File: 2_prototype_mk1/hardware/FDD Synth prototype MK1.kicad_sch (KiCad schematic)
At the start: 3 parts, among them J3 Conn_01x04_Pin

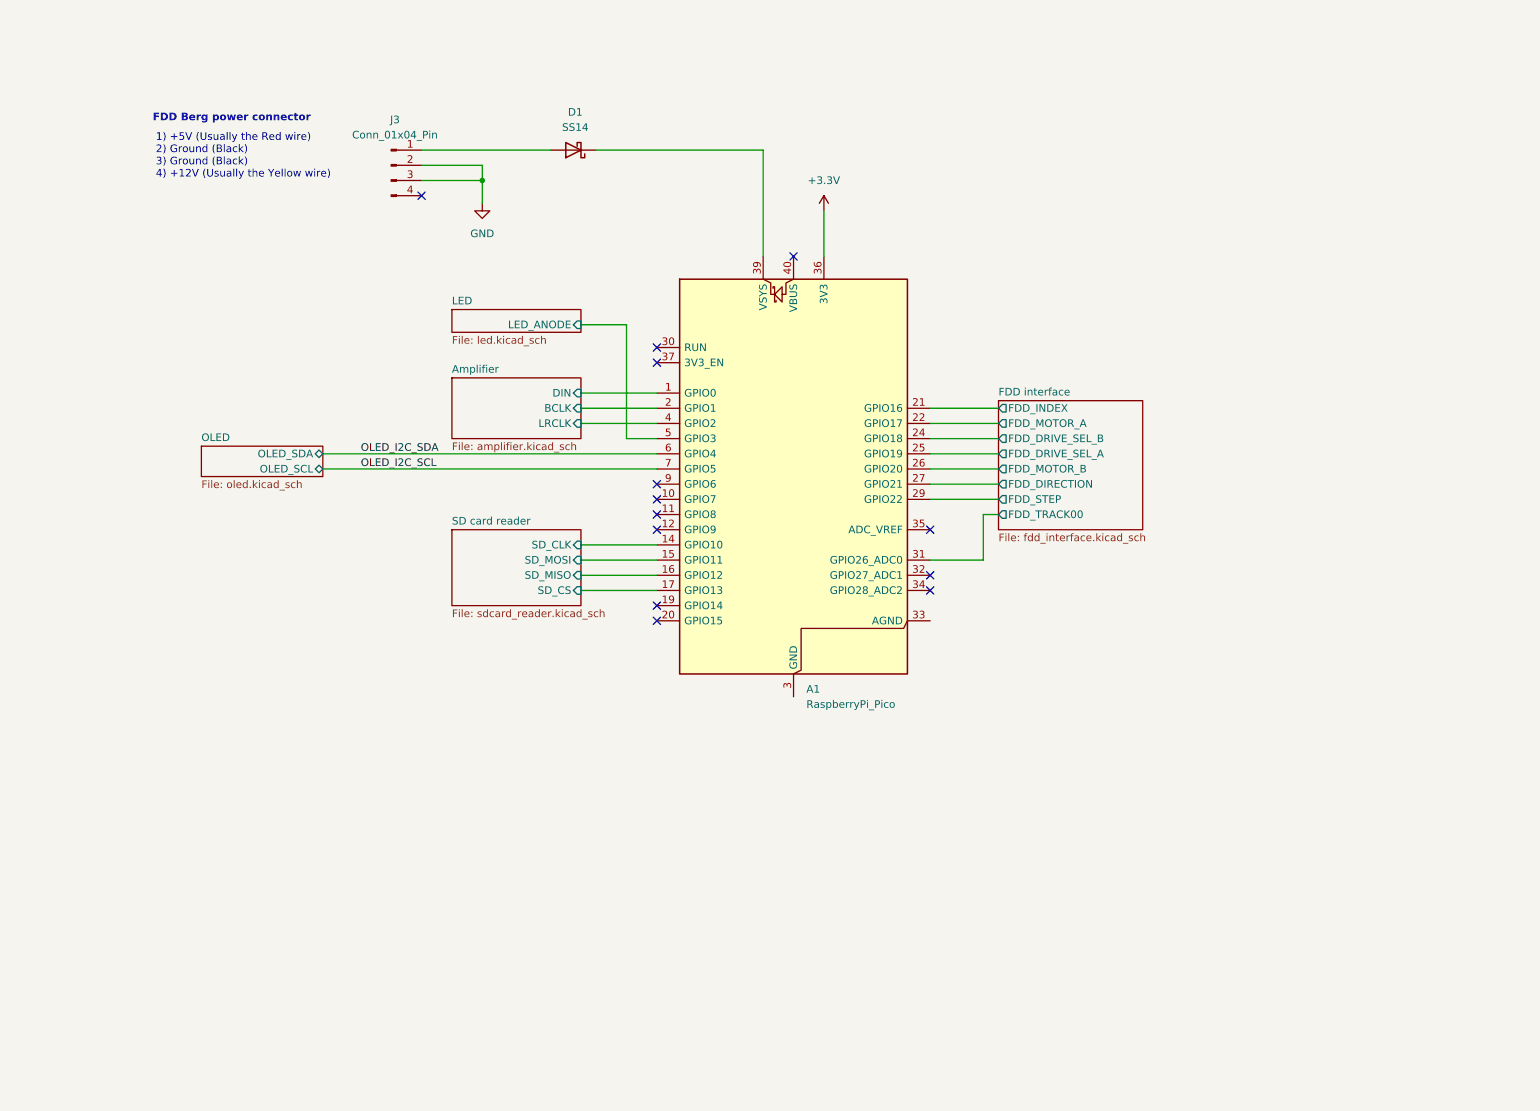
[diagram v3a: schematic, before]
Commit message: Quick and dirty layout of traces - not final
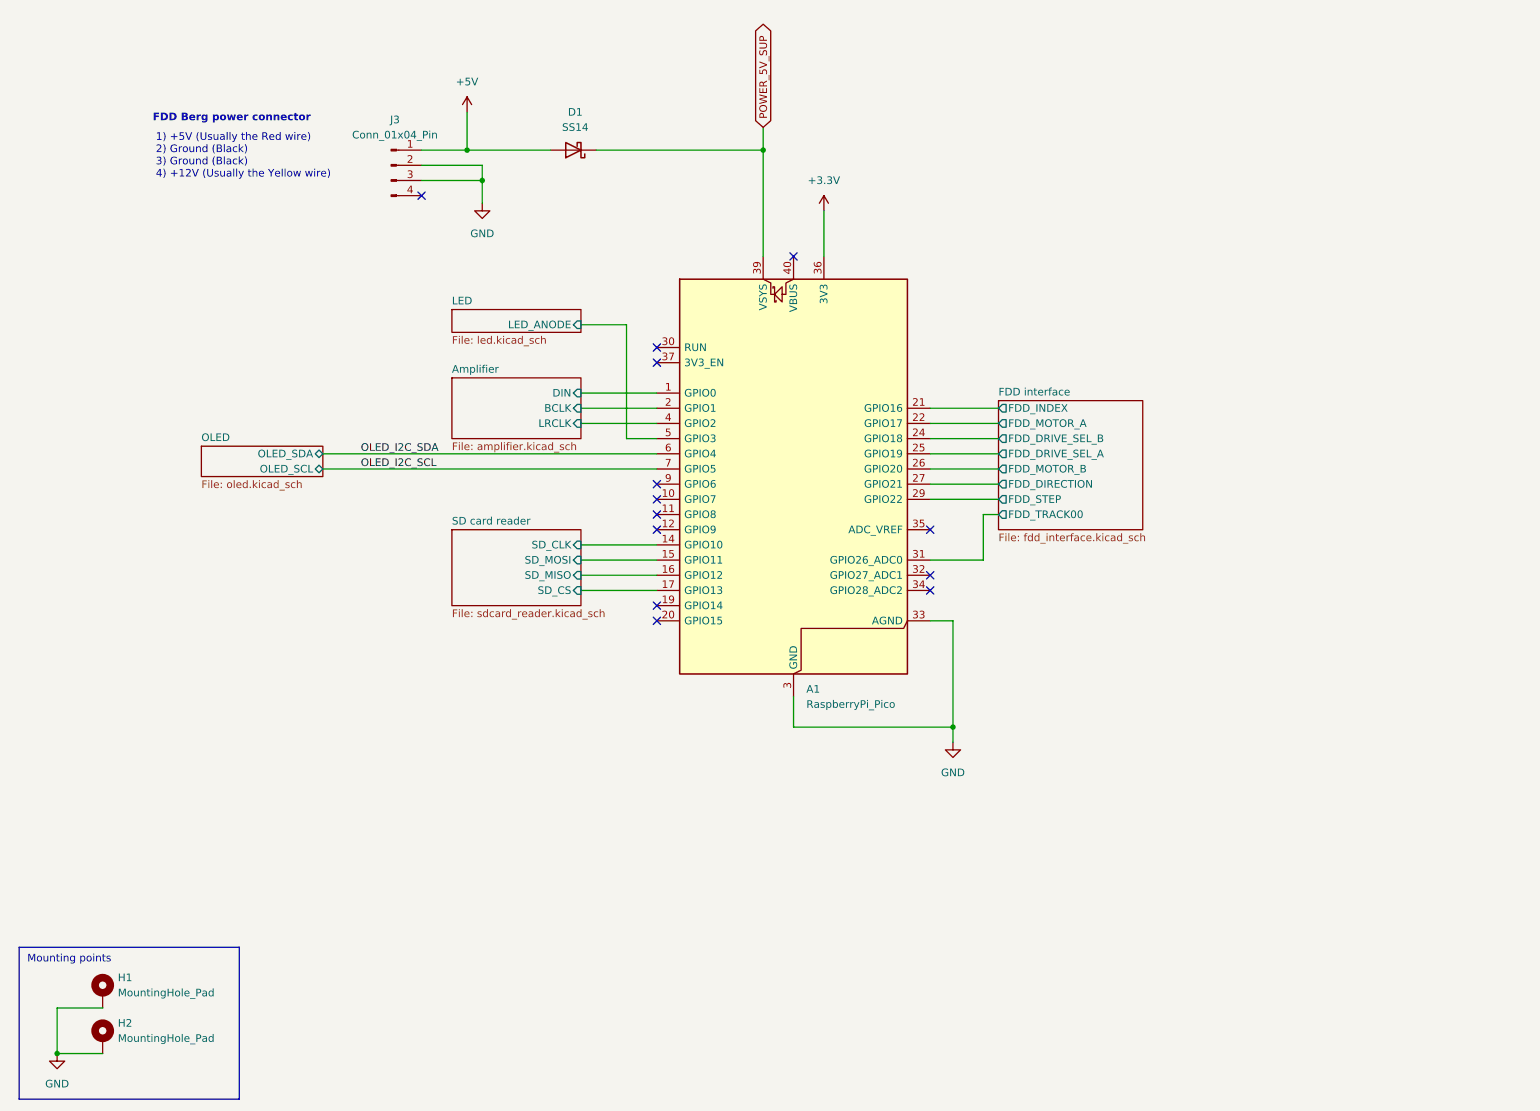
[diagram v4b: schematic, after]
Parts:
- added H1, H2: MountingHole_Pad, MountingHole:MountingHole_3.2mm_M3_Pad_Via, symbol Mechanical:MountingHole_Pad
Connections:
- net GND: now also A1.13 (GND), A1.18 (GND), A1.23 (GND), A1.28 (GND), A1.3 (GND), A1.33 (AGND), A1.38 (GND), A1.8 (GND), H1.1, H2.1
- net POWER_5V_SUP: now reaches A1.39 (VSYS), D1.1 (K)
- net +5V: now reaches D1.2 (A), J3.1 (Pin_1)
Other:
- note added: "Mounting points"

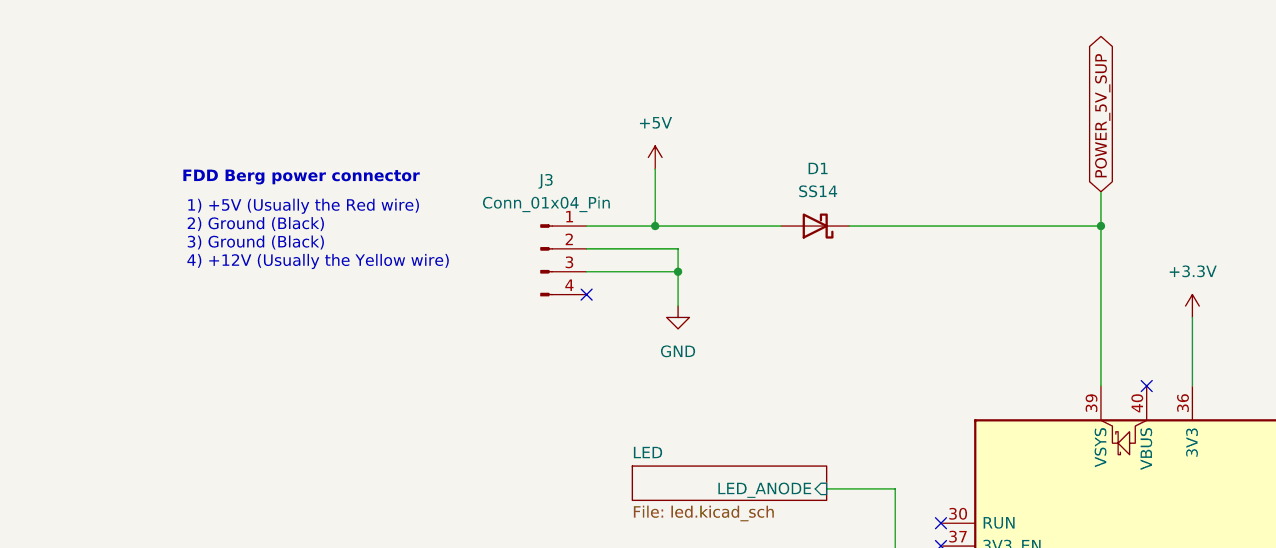
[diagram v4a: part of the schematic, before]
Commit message: Split power into own schematic
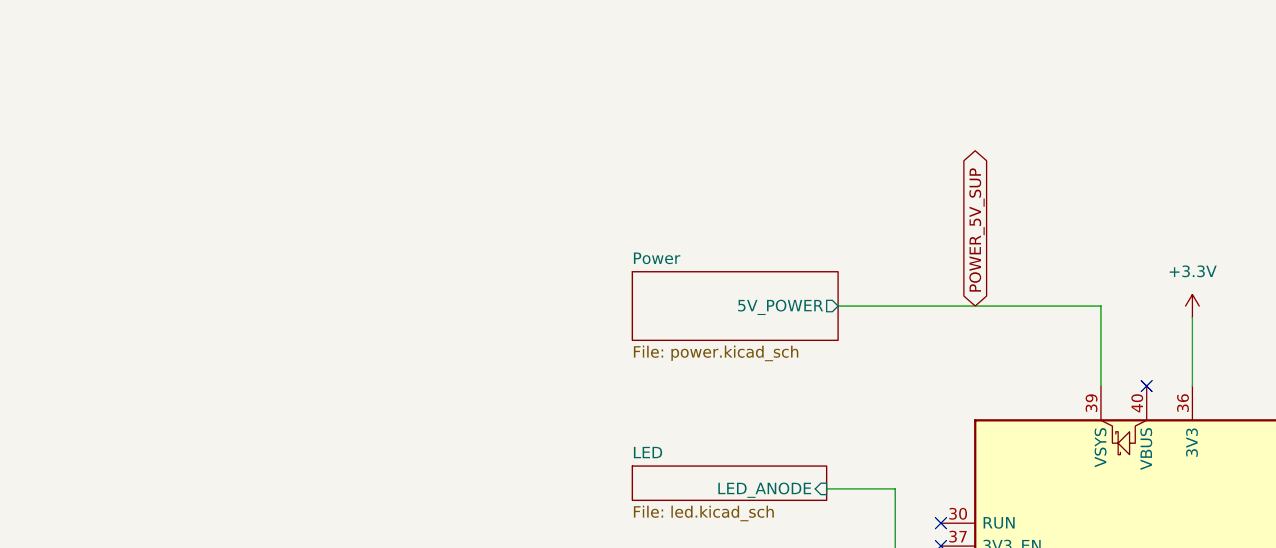
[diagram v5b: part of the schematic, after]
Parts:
- removed D1: SS14, Diode_SMD:D_SMA, symbol Device:D_Schottky
- removed J3: Conn_01x04_Pin, Connector_JST:JST_XH_B4B-XH-A_1x04_P2.50mm_Vertical, symbol Connector:Conn_01x04_Pin
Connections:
- no-connect marks 13 -> 12
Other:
- added sheet Power (power.kicad_sch)
- note removed: "1) +5V (Usually the Red wire) 2) Ground (Black) 3) Ground (Black) 4) +12V (Usually the Yellow wire)"
- note removed: "FDD Berg power connector"

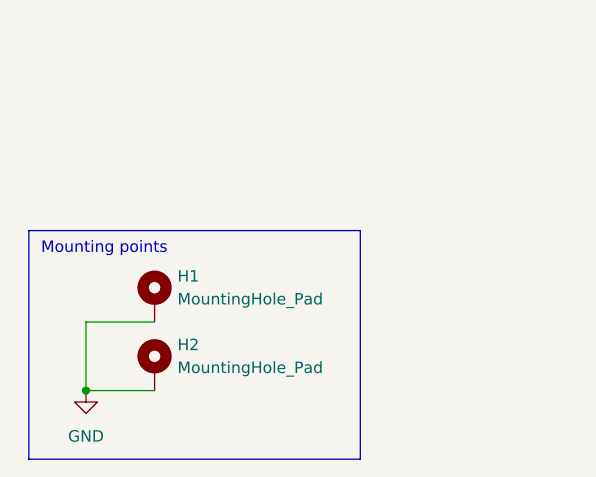
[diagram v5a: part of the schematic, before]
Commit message: Change power connector and reroute amp
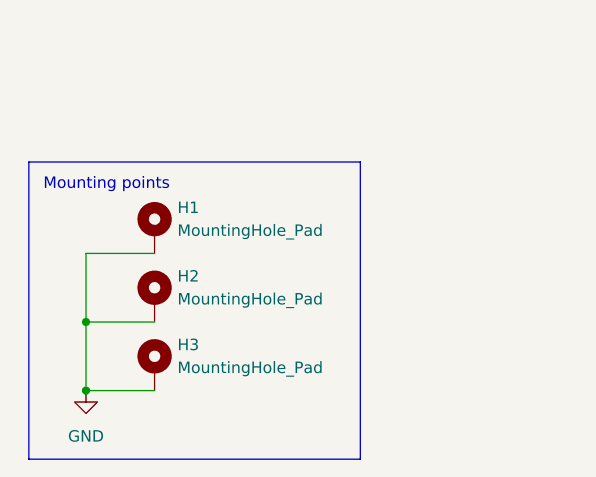
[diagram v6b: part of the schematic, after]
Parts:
- added H3: MountingHole_Pad, MountingHole:MountingHole_3.2mm_M3_Pad_Via, symbol Mechanical:MountingHole_Pad
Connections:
- net GND: now also H3.1
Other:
- moved on the sheet: H1, H2
